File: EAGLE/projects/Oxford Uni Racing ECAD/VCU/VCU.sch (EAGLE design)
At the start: 24 parts, among them J1 PWR_CAN, J2 PWR_CAN, J3 MC_LEFT, J4 MC_RIGHT, K1 RT444012, X2 D-SUB9-H2M09ST

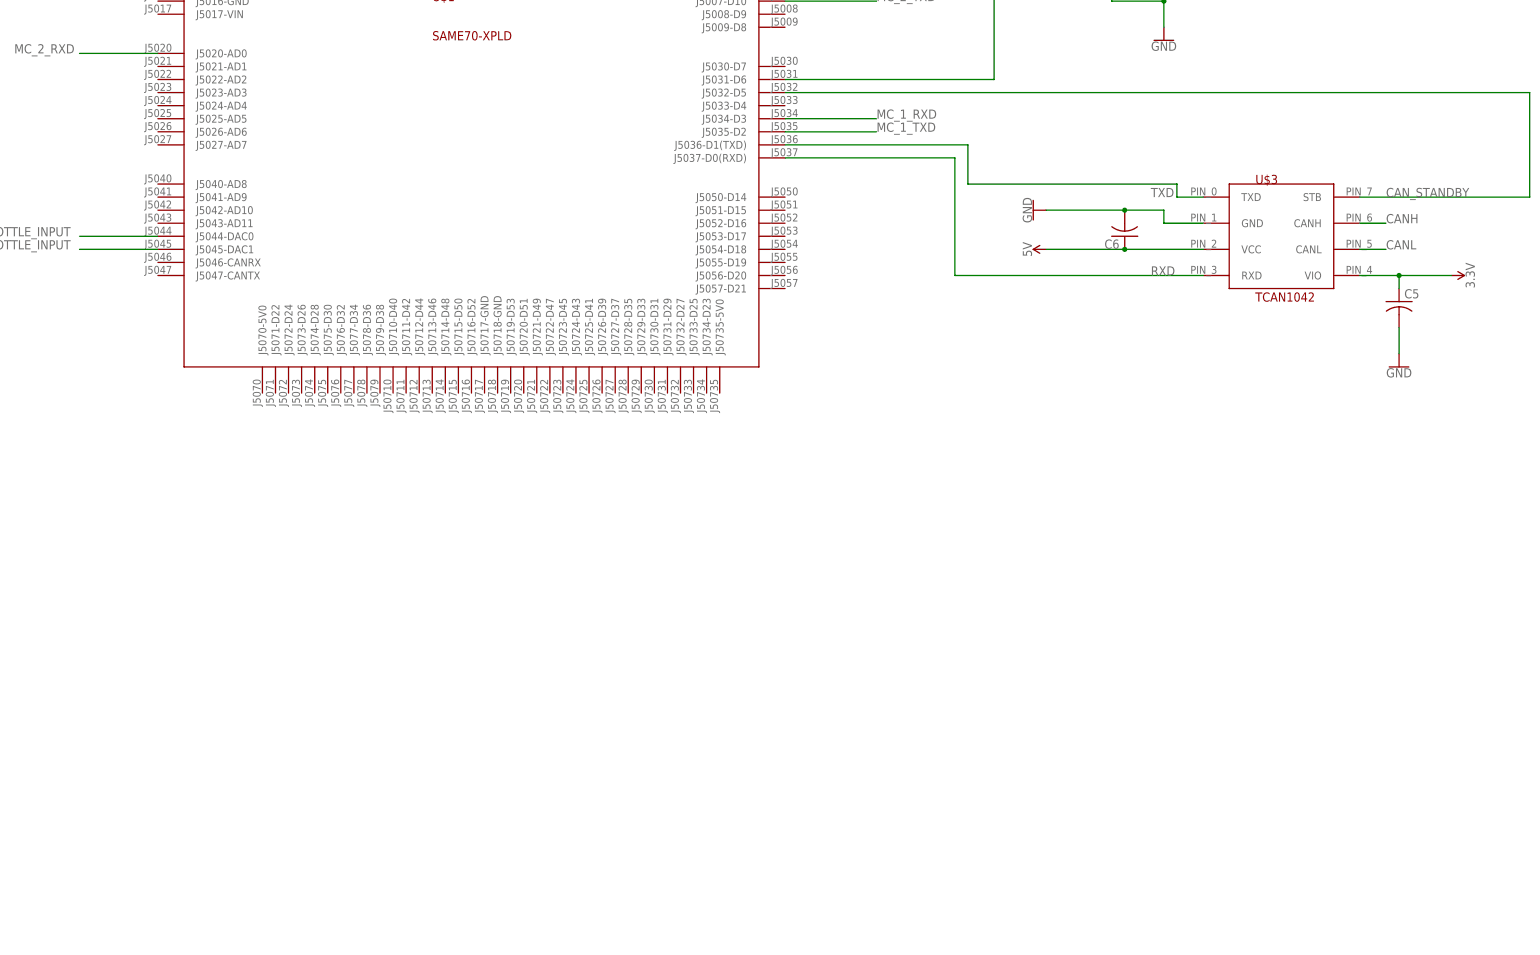
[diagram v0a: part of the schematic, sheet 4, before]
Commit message: fixed can wiring on VCU
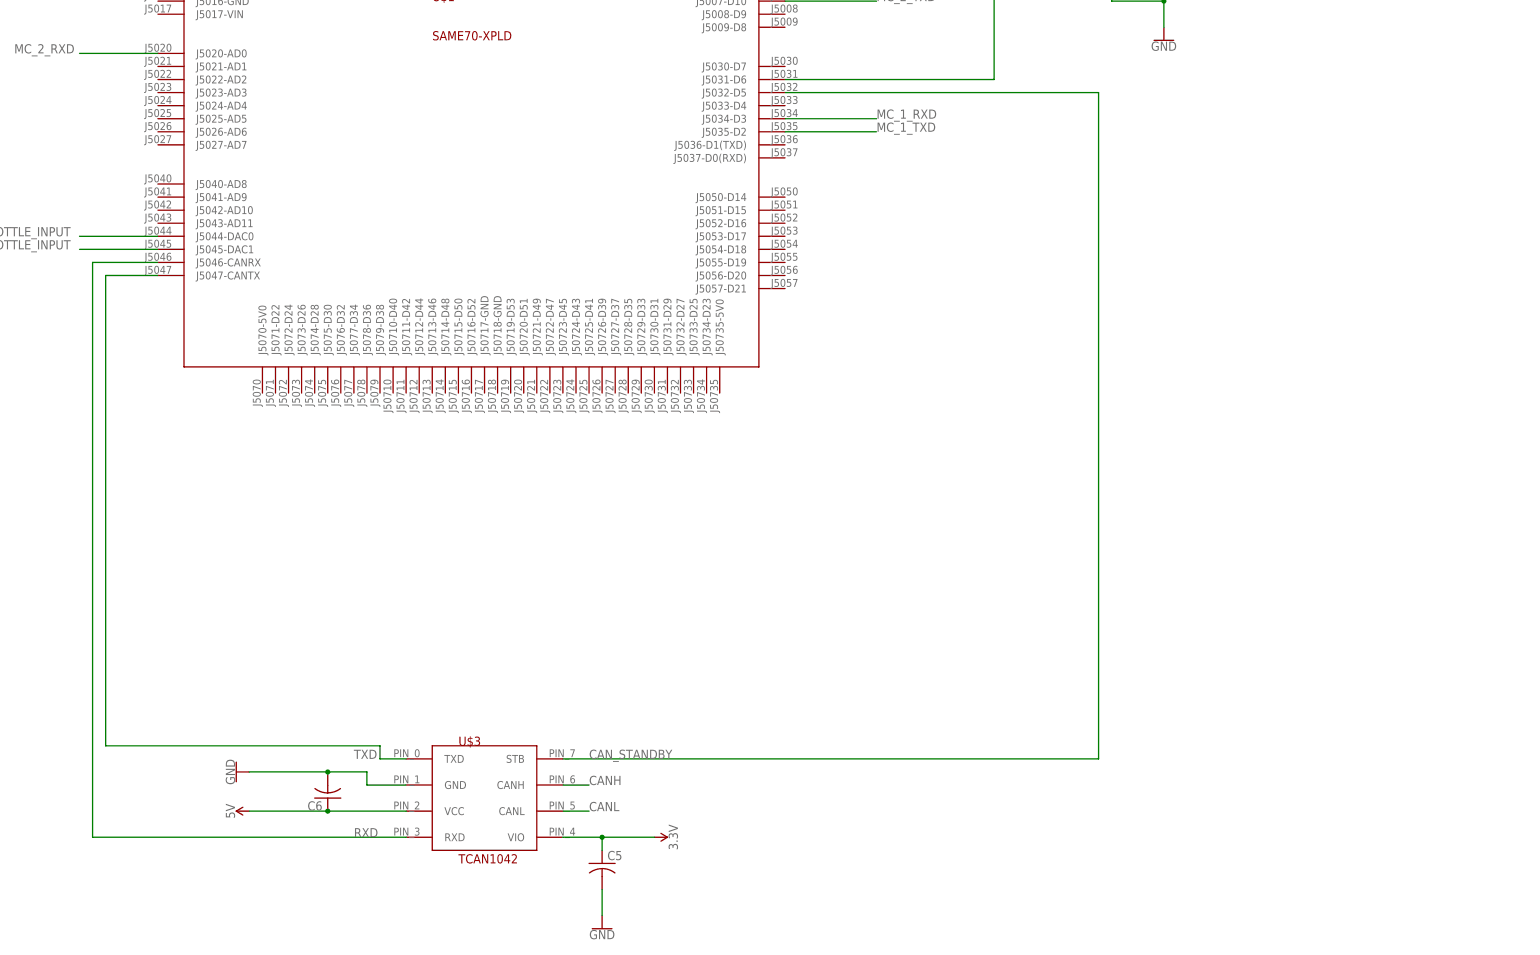
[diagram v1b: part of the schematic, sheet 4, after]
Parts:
- J2: value PWR_CAN -> ASS
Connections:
- net RXD: now also U$1.J5046-CANRX; no longer U$1.J5037-D0(RXD)
- net TXD: now also U$1.J5047-CANTX; no longer U$1.J5036-D1(TXD)
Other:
- moved on the sheet: C5, C6, U$3
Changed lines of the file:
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@@
 <part name="SUPPLY26" library="SparkFun-PowerSymbols" library_urn="urn:adsk.eagle:library:530" deviceset="12V" device=""/>
 <part name="GND20" library="SparkFun-PowerSymbols" library_urn="urn:adsk.eagle:library:530" deviceset="GND" device=""/>
-<part name="J2" library="T821108A1S100CEU" deviceset="T821108A1S100CEU" device="" value="PWR_CAN"/>
+<part name="J2" library="T821108A1S100CEU" deviceset="T821108A1S100CEU" device="" value="ASS"/>
 </parts>
 <sheets>
@@
 <attribute name="VALUE" x="218.44" y="88.9" size="1.778" layer="94"/>
 </instance>
-<instance part="U$3" gate="G$1" x="358.14" y="40.64" smashed="yes">
-<attribute name="NAME" x="378.46" y="60.96" size="1.778" layer="94"/>
-<attribute name="VALUE" x="378.46" y="38.1" size="1.778" layer="94"/>
-</instance>
-<instance part="C5" gate="G$1" x="406.4" y="38.1" smashed="yes">
-<attribute name="NAME" x="407.416" y="38.735" size="1.778" layer="95"/>
-<attribute name="VALUE" x="407.416" y="33.909" size="1.778" layer="96"/>
-</instance>
-<instance part="C6" gate="G$1" x="353.06" y="50.8" smashed="yes" rot="R180">
-<attribute name="NAME" x="352.044" y="50.165" size="1.778" layer="95" rot="R180"/>
-<attribute name="VALUE" x="352.044" y="54.991" size="1.778" layer="96" rot="R180"/>
-</instance>
-<instance part="SUPPLY30" gate="G$1" x="337.82" y="48.26" smashed="yes" rot="R90">
-<attribute name="VALUE" x="335.026" y="48.26" size="1.778" layer="96" rot="R90" align="bottom-center"/>
-</instance>
-<instance part="GND22" gate="1" x="335.28" y="55.88" smashed="yes" rot="R270">
-<attribute name="VALUE" x="335.026" y="55.88" size="1.778" layer="96" rot="R270" align="top-center"/>
-</instance>
-<instance part="GND23" gate="1" x="406.4" y="25.4" smashed="yes">
-<attribute name="VALUE" x="406.4" y="25.146" size="1.778" layer="96" align="top-center"/>
-</instance>
-<instance part="SUPPLY31" gate="G$1" x="416.56" y="43.18" smashed="yes" rot="R270">
-<attribute name="VALUE" x="419.354" y="43.18" size="1.778" layer="96" rot="R270" align="bottom-center"/>
+<instance part="U$3" gate="G$1" x="203.2" y="-68.58" smashed="yes">
+<attribute name="NAME" x="223.52" y="-48.26" size="1.778" layer="94"/>
+<attribute name="VALUE" x="223.52" y="-71.12" size="1.778" layer="94"/>
+</instance>
+<instance part="C5" gate="G$1" x="251.46" y="-71.12" smashed="yes">
+<attribute name="NAME" x="252.476" y="-70.485" size="1.778" layer="95"/>
+<attribute name="VALUE" x="252.476" y="-75.311" size="1.778" layer="96"/>
+</instance>
+<instance part="C6" gate="G$1" x="198.12" y="-58.42" smashed="yes" rot="R180">
+<attribute name="NAME" x="197.104" y="-59.055" size="1.778" layer="95" rot="R180"/>
+<attribute name="VALUE" x="197.104" y="-54.229" size="1.778" layer="96" rot="R180"/>
+</instance>
+<instance part="SUPPLY30" gate="G$1" x="182.88" y="-60.96" smashed="yes" rot="R90">
+<attribute name="VALUE" x="180.086" y="-60.96" size="1.778" layer="96" rot="R90" align="bottom-center"/>
+</instance>
+<instance part="GND22" gate="1" x="180.34" y="-53.34" smashed="yes" rot="R270">
+<attribute name="VALUE" x="180.086" y="-53.34" size="1.778" layer="96" rot="R270" align="top-center"/>
+</instance>
+<instance part="GND23" gate="1" x="251.46" y="-83.82" smashed="yes">
+<attribute name="VALUE" x="251.46" y="-84.074" size="1.778" layer="96" align="top-center"/>
+</instance>
+<instance part="SUPPLY31" gate="G$1" x="261.62" y="-66.04" smashed="yes" rot="R270">
+<attribute name="VALUE" x="264.414" y="-66.04" size="1.778" layer="96" rot="R270" align="bottom-center"/>
 </instance>
 <instance part="BR_LIGHTS_TR" gate="G$1" x="358.14" y="116.84" smashed="yes">
@@
 <pinref part="U$3" gate="G$1" pin="VCC"/>
 <pinref part="C6" gate="G$1" pin="1"/>
-<wire x1="368.3" y1="48.26" x2="353.06" y2="48.26" width="0.1524" layer="91"/>
+<wire x1="213.36" y1="-60.96" x2="198.12" y2="-60.96" width="0.1524" layer="91"/>
 <pinref part="SUPPLY30" gate="G$1" pin="5V"/>
-<wire x1="337.82" y1="48.26" x2="353.06" y2="48.26" width="0.1524" layer="91"/>
-<junction x="353.06" y="48.26"/>
+<wire x1="182.88" y1="-60.96" x2="198.12" y2="-60.96" width="0.1524" layer="91"/>
+<junction x="198.12" y="-60.96"/>
 </segment>
 </net>
@@
 <pinref part="U$3" gate="G$1" pin="VIO"/>
 <pinref part="SUPPLY31" gate="G$1" pin="3.3V"/>
-<wire x1="398.78" y1="43.18" x2="406.4" y2="43.18" width="0.1524" layer="91"/>
+<wire x1="243.84" y1="-66.04" x2="251.46" y2="-66.04" width="0.1524" layer="91"/>
 <pinref part="C5" gate="G$1" pin="1"/>
-<wire x1="406.4" y1="43.18" x2="416.56" y2="43.18" width="0.1524" layer="91"/>
-<wire x1="406.4" y1="40.64" x2="406.4" y2="43.18" width="0.1524" layer="91"/>
-<junction x="406.4" y="43.18"/>
+<wire x1="251.46" y1="-66.04" x2="261.62" y2="-66.04" width="0.1524" layer="91"/>
+<wire x1="251.46" y1="-68.58" x2="251.46" y2="-66.04" width="0.1524" layer="91"/>
+<junction x="251.46" y="-66.04"/>
 </segment>
 </net>
@@
 <pinref part="GND22" gate="1" pin="GND"/>
 <pinref part="C6" gate="G$1" pin="2"/>
-<wire x1="337.82" y1="55.88" x2="353.06" y2="55.88" width="0.1524" layer="91"/>
-<wire x1="353.06" y1="55.88" x2="360.68" y2="55.88" width="0.1524" layer="91"/>
-<junction x="353.06" y="55.88"/>
-<wire x1="360.68" y1="55.88" x2="360.68" y2="53.34" width="0.1524" layer="91"/>
+<wire x1="182.88" y1="-53.34" x2="198.12" y2="-53.34" width="0.1524" layer="91"/>
+<wire x1="198.12" y1="-53.34" x2="205.74" y2="-53.34" width="0.1524" layer="91"/>
+<junction x="198.12" y="-53.34"/>
+<wire x1="205.74" y1="-53.34" x2="205.74" y2="-55.88" width="0.1524" layer="91"/>
 <pinref part="U$3" gate="G$1" pin="GND"/>
-<wire x1="360.68" y1="53.34" x2="368.3" y2="53.34" width="0.1524" layer="91"/>
+<wire x1="205.74" y1="-55.88" x2="213.36" y2="-55.88" width="0.1524" layer="91"/>
 </segment>
 <segment>
 <pinref part="GND23" gate="1" pin="GND"/>
 <pinref part="C5" gate="G$1" pin="2"/>
-<wire x1="406.4" y1="27.94" x2="406.4" y2="33.02" width="0.1524" layer="91"/>
+<wire x1="251.46" y1="-81.28" x2="251.46" y2="-76.2" width="0.1524" layer="91"/>
 </segment>
 <segment>
@@
 <segment>
 <pinref part="U$3" gate="G$1" pin="CANH"/>
-<wire x1="398.78" y1="53.34" x2="403.86" y2="53.34" width="0.1524" layer="91"/>
-<label x="403.86" y="53.34" size="1.778" layer="95"/>
+<wire x1="243.84" y1="-55.88" x2="248.92" y2="-55.88" width="0.1524" layer="91"/>
+<label x="248.92" y="-55.88" size="1.778" layer="95"/>
 </segment>
 </net>
@@
 <segment>
 <pinref part="U$3" gate="G$1" pin="CANL"/>
-<wire x1="398.78" y1="48.26" x2="403.86" y2="48.26" width="0.1524" layer="91"/>
-<label x="403.86" y="48.26" size="1.778" layer="95"/>
+<wire x1="243.84" y1="-60.96" x2="248.92" y2="-60.96" width="0.1524" layer="91"/>
+<label x="248.92" y="-60.96" size="1.778" layer="95"/>
 </segment>
 </net>
@@
 <segment>
 <pinref part="U$3" gate="G$1" pin="STB"/>
-<label x="403.86" y="58.42" size="1.778" layer="95"/>
+<label x="248.92" y="-50.8" size="1.778" layer="95"/>
 <pinref part="U$1" gate="G$1" pin="J5032-D5"/>
-<wire x1="287.02" y1="78.74" x2="431.8" y2="78.74" width="0.1524" layer="91"/>
-<wire x1="431.8" y1="78.74" x2="431.8" y2="58.42" width="0.1524" layer="91"/>
-<wire x1="431.8" y1="58.42" x2="398.78" y2="58.42" width="0.1524" layer="91"/>
+<wire x1="287.02" y1="78.74" x2="347.98" y2="78.74" width="0.1524" layer="91"/>
+<wire x1="347.98" y1="78.74" x2="347.98" y2="-50.8" width="0.1524" layer="91"/>
+<wire x1="347.98" y1="-50.8" x2="243.84" y2="-50.8" width="0.1524" layer="91"/>
 </segment>
 </net>
@@
 <segment>
 <pinref part="U$3" gate="G$1" pin="TXD"/>
-<label x="358.14" y="58.42" size="1.778" layer="95"/>
-<pinref part="U$1" gate="G$1" pin="J5036-D1(TXD)"/>
-<wire x1="287.02" y1="68.58" x2="322.58" y2="68.58" width="0.1524" layer="91"/>
-<wire x1="322.58" y1="68.58" x2="322.58" y2="60.96" width="0.1524" layer="91"/>
-<wire x1="322.58" y1="60.96" x2="363.22" y2="60.96" width="0.1524" layer="91"/>
-<wire x1="363.22" y1="60.96" x2="363.22" y2="58.42" width="0.1524" layer="91"/>
-<wire x1="363.22" y1="58.42" x2="368.3" y2="58.42" width="0.1524" layer="91"/>
+<label x="203.2" y="-50.8" size="1.778" layer="95"/>
+<wire x1="154.94" y1="-48.26" x2="208.28" y2="-48.26" width="0.1524" layer="91"/>
+<wire x1="208.28" y1="-48.26" x2="208.28" y2="-50.8" width="0.1524" layer="91"/>
+<wire x1="208.28" y1="-50.8" x2="213.36" y2="-50.8" width="0.1524" layer="91"/>
+<pinref part="U$1" gate="G$1" pin="J5047-CANTX"/>
+<wire x1="165.1" y1="43.18" x2="154.94" y2="43.18" width="0.1524" layer="91"/>
+<wire x1="154.94" y1="43.18" x2="154.94" y2="-48.26" width="0.1524" layer="91"/>
 </segment>
 </net>
@@
 <segment>
 <pinref part="U$3" gate="G$1" pin="RXD"/>
-<label x="358.14" y="43.18" size="1.778" layer="95"/>
-<pinref part="U$1" gate="G$1" pin="J5037-D0(RXD)"/>
-<wire x1="287.02" y1="66.04" x2="320.04" y2="66.04" width="0.1524" layer="91"/>
-<wire x1="320.04" y1="66.04" x2="320.04" y2="43.18" width="0.1524" layer="91"/>
-<wire x1="320.04" y1="43.18" x2="368.3" y2="43.18" width="0.1524" layer="91"/>
-</segment>
-</net>
+<label x="203.2" y="-66.04" size="1.778" layer="95"/>
+<wire x1="152.4" y1="-66.04" x2="213.36" y2="-66.04" width="0.1524" layer="91"/>
+<pinref part="U$1" gate="G$1" pin="J5046-CANRX"/>
+<wire x1="152.4" y1="-66.04" x2="152.4" y2="45.72" width="0.1524" layer="91"/>
+<wire x1="152.4" y1="45.72" x2="165.1" y2="45.72" width="0.1524" layer="91"/>
+</segment>
+</net>

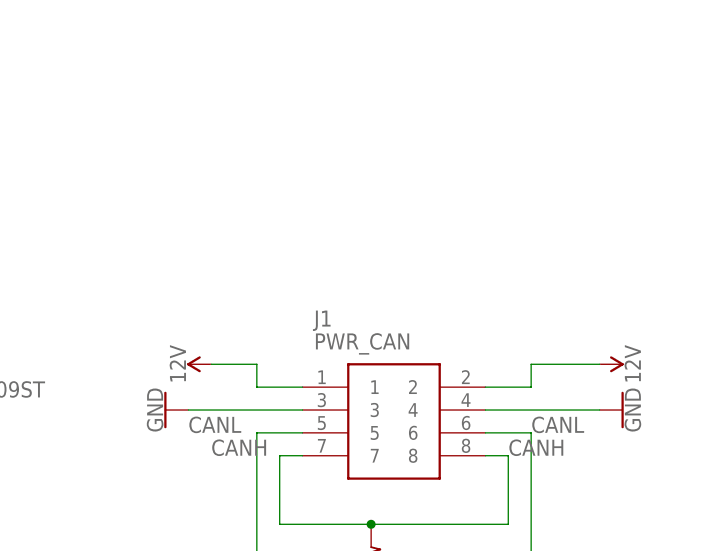
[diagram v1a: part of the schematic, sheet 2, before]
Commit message: added fuses to boards
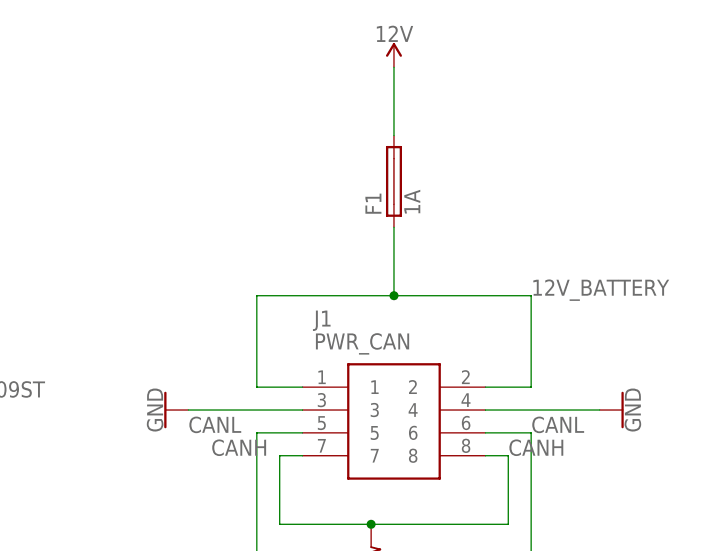
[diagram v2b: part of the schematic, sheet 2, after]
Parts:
- added F1: 1A, fuse:FUSEBLANK_5X20MM
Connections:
- new net 12V_BATTERY: F1.1, J1.1, J1.2
- net 12V: now also F1.2; no longer J1.1, J1.2
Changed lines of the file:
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@@
 <part name="GND6" library="SparkFun-PowerSymbols" library_urn="urn:adsk.eagle:library:530" deviceset="GND" device=""/>
 <part name="X2" library="con-thomas-betts" library_urn="urn:adsk.eagle:library:191" deviceset="D-SUB9-" device="H2M09ST" package3d_urn="urn:adsk.eagle:package:10567/1"/>
-<part name="SUPPLY22" library="SparkFun-PowerSymbols" library_urn="urn:adsk.eagle:library:530" deviceset="12V" device=""/>
 <part name="GND10" library="SparkFun-PowerSymbols" library_urn="urn:adsk.eagle:library:530" deviceset="GND" device=""/>
 <part name="SUPPLY23" library="SparkFun-PowerSymbols" library_urn="urn:adsk.eagle:library:530" deviceset="5V" device=""/>
@@
 <part name="GND20" library="SparkFun-PowerSymbols" library_urn="urn:adsk.eagle:library:530" deviceset="GND" device=""/>
 <part name="J2" library="T821108A1S100CEU" deviceset="T821108A1S100CEU" device="" value="ASS"/>
+<part name="F1" library="fuse" library_urn="urn:adsk.eagle:library:233" deviceset="FUSE" device="BLANK_5X20MM" package3d_urn="urn:adsk.eagle:package:14079/1" value="1A"/>
 </parts>
 <sheets>
@@
 <attribute name="NAME" x="102.87" y="77.978" size="1.778" layer="95"/>
 </instance>
-<instance part="SUPPLY22" gate="G$1" x="180.34" y="104.14" smashed="yes" rot="R270">
-<attribute name="VALUE" x="183.134" y="104.14" size="1.778" layer="96" rot="R270" align="bottom-center"/>
-</instance>
 <instance part="GND10" gate="1" x="182.88" y="99.06" smashed="yes" rot="R90">
 <attribute name="VALUE" x="183.134" y="99.06" size="1.778" layer="96" rot="R90" align="top-center"/>
@@
 <attribute name="VALUE" x="78.486" y="91.44" size="1.778" layer="96" rot="R270" align="top-center"/>
 </instance>
-<instance part="SUPPLY24" gate="G$1" x="137.16" y="104.14" smashed="yes" rot="R90">
-<attribute name="VALUE" x="134.366" y="104.14" size="1.778" layer="96" rot="R90" align="bottom-center"/>
+<instance part="SUPPLY24" gate="G$1" x="157.48" y="137.16" smashed="yes">
+<attribute name="VALUE" x="157.48" y="139.954" size="1.778" layer="96" align="bottom-center"/>
 </instance>
 <instance part="GND12" gate="1" x="132.08" y="99.06" smashed="yes" rot="R270">
@@
 <attribute name="NAME" x="148.59" y="60.96" size="1.778" layer="95" align="center-left"/>
 <attribute name="VALUE" x="148.59" y="58.42" size="1.778" layer="96" align="center-left"/>
+</instance>
+<instance part="F1" gate="G$1" x="157.48" y="124.46" smashed="yes" rot="R90">
+<attribute name="NAME" x="156.083" y="120.65" size="1.778" layer="95" rot="R90"/>
+<attribute name="VALUE" x="160.401" y="120.65" size="1.778" layer="96" rot="R90"/>
 </instance>
 </instances>
@@
 </segment>
 <segment>
-<wire x1="147.32" y1="101.6" x2="142.24" y2="101.6" width="0.1524" layer="91"/>
-<wire x1="142.24" y1="101.6" x2="142.24" y2="104.14" width="0.1524" layer="91"/>
+<pinref part="F1" gate="G$1" pin="2"/>
 <pinref part="SUPPLY24" gate="G$1" pin="12V"/>
-<wire x1="142.24" y1="104.14" x2="137.16" y2="104.14" width="0.1524" layer="91"/>
-<pinref part="J1" gate="G$1" pin="1"/>
-</segment>
-<segment>
-<wire x1="167.64" y1="101.6" x2="172.72" y2="101.6" width="0.1524" layer="91"/>
-<wire x1="172.72" y1="101.6" x2="172.72" y2="104.14" width="0.1524" layer="91"/>
-<pinref part="SUPPLY22" gate="G$1" pin="12V"/>
-<wire x1="172.72" y1="104.14" x2="180.34" y2="104.14" width="0.1524" layer="91"/>
-<pinref part="J1" gate="G$1" pin="2"/>
+<wire x1="157.48" y1="129.54" x2="157.48" y2="137.16" width="0.1524" layer="91"/>
 </segment>
 </net>
@@
 </segment>
 </net>
+<net name="12V_BATTERY" class="0">
+<segment>
+<wire x1="147.32" y1="101.6" x2="142.24" y2="101.6" width="0.1524" layer="91"/>
+<pinref part="J1" gate="G$1" pin="1"/>
+<wire x1="142.24" y1="101.6" x2="142.24" y2="111.76" width="0.1524" layer="91"/>
+<wire x1="142.24" y1="111.76" x2="157.48" y2="111.76" width="0.1524" layer="91"/>
+<wire x1="157.48" y1="111.76" x2="172.72" y2="111.76" width="0.1524" layer="91"/>
+<wire x1="167.64" y1="101.6" x2="172.72" y2="101.6" width="0.1524" layer="91"/>
+<pinref part="J1" gate="G$1" pin="2"/>
+<wire x1="172.72" y1="111.76" x2="172.72" y2="101.6" width="0.1524" layer="91"/>
+<pinref part="F1" gate="G$1" pin="1"/>
+<wire x1="157.48" y1="111.76" x2="157.48" y2="119.38" width="0.1524" layer="91"/>
+<junction x="157.48" y="111.76"/>
+<label x="172.72" y="111.76" size="1.778" layer="95"/>
+</segment>
+</net>
